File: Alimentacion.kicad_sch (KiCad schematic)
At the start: 0 parts

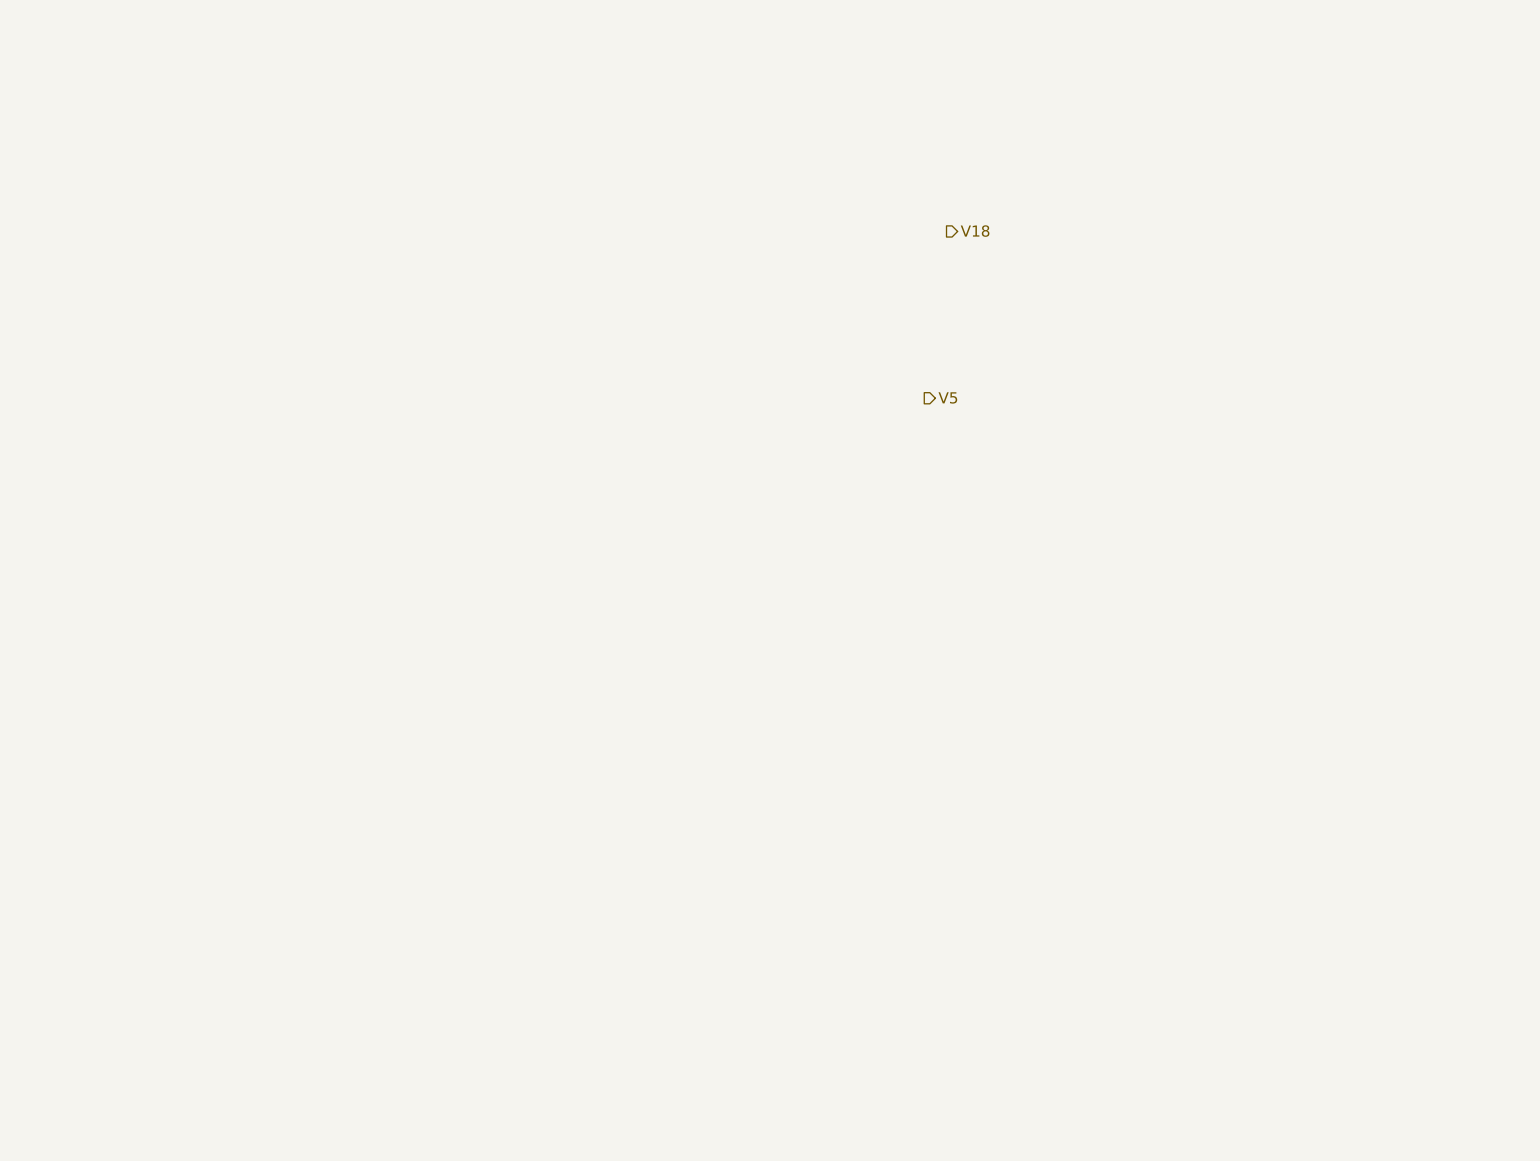
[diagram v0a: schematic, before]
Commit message: Branch Alimentacion 1.1 Modificaciones para que la alimentacion sea adecuada.
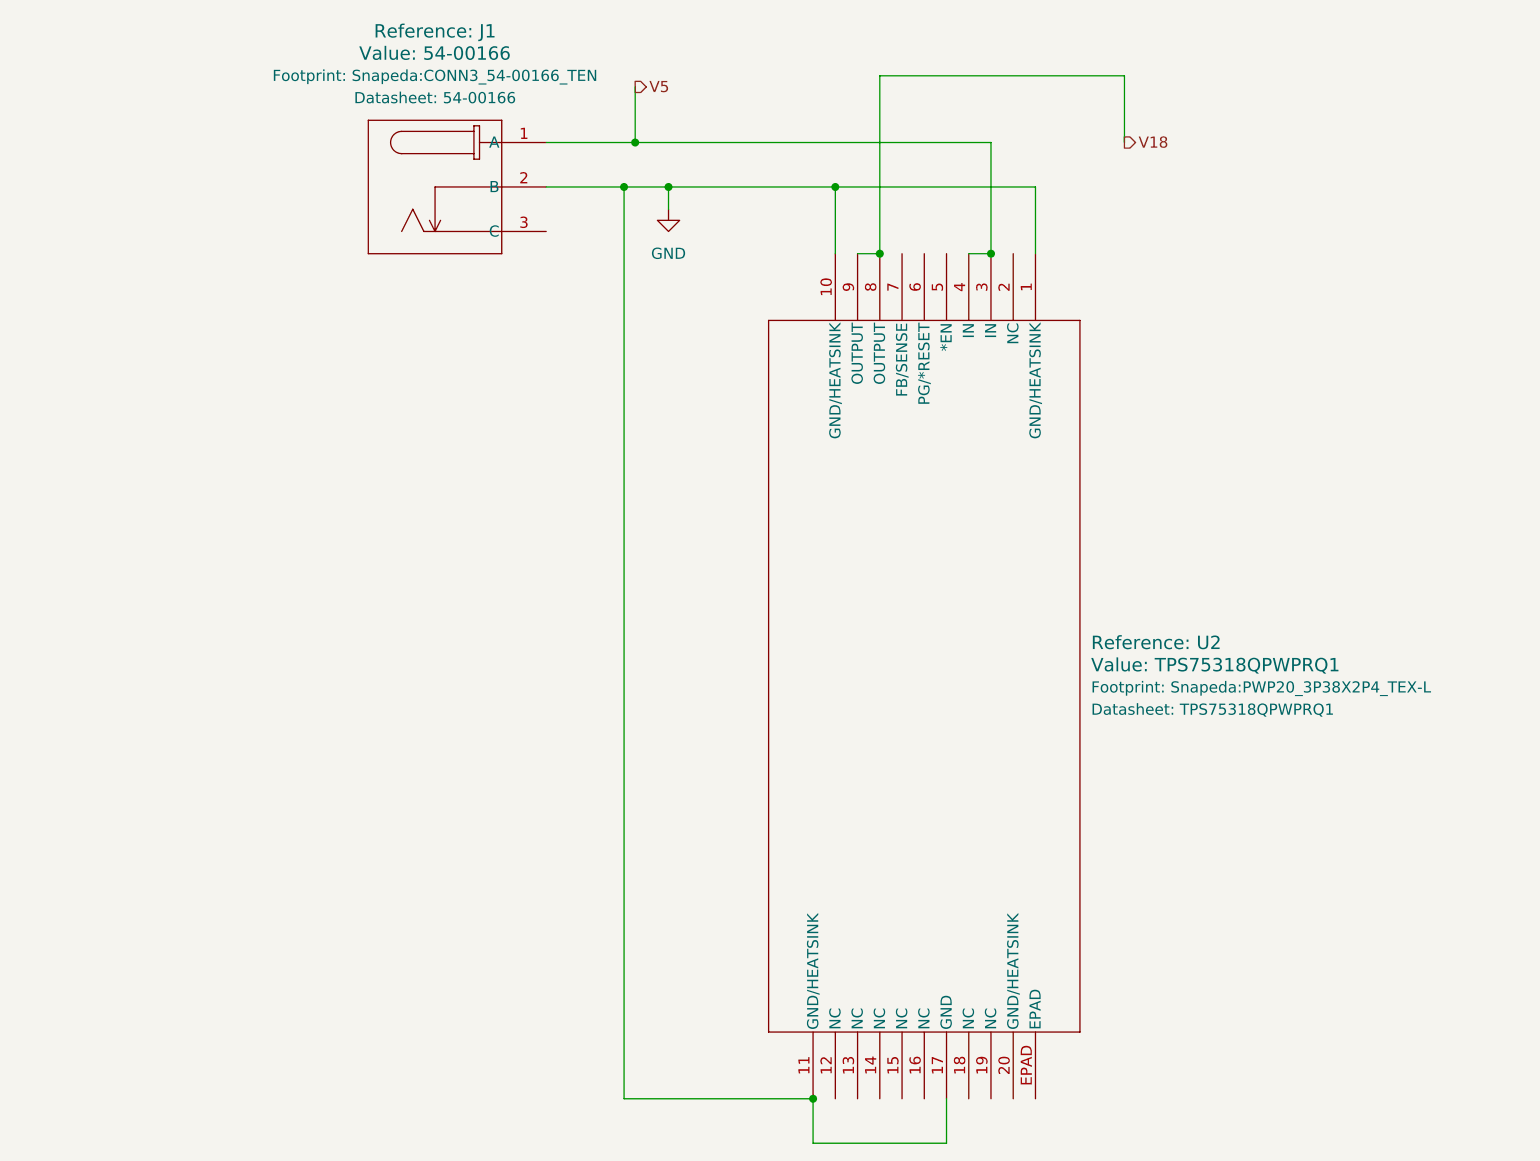
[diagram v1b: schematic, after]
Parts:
- added J1: 54-00166, Snapeda:CONN3_54-00166_TEN, symbol Snapeda:54-00166
- added U2: TPS75318QPWPRQ1, Snapeda:PWP20_3P38X2P4_TEX-L, symbol Snapeda:TPS75318QPWPRQ1
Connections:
- net V18: now also U2.8 (OUTPUT), U2.9 (OUTPUT)
- net V5: now also J1.1 (A), U2.3 (IN), U2.4 (IN)
- new net GND: J1.2 (B), U2.1 (GND/HEATSINK), U2.10 (GND/HEATSINK), U2.11 (GND/HEATSINK), U2.17 (GND)

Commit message: Alimentacion v1.2 Completamos los MPN de la hoja Alimentacion
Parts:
- J1: MPN (none) -> 54-00166
- U2: MPN (none) -> TPS75318QPWPRQ1
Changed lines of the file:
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@@
+			)
+		)
+		(property "MPN" "54-00166"
+			(at 62.23 49.53 0)
+			(hide yes)
+			(show_name no)
+			(do_not_autoplace no)
+			(effects
+				(font
+					(size 1.27 1.27)
+				)
 			)
 		)
@@
 			(do_not_autoplace no)
 			(effects
+				(font
+					(size 1.27 1.27)
+				)
+			)
+		)
+		(property "MPN" "TPS75318QPWPRQ1"
+			(at 118.11 62.23 90)
+			(hide yes)
+			(show_name no)
+			(do_not_autoplace no)
+			(effects

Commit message: -Version 1.4
Arreglos en el esquematico
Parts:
- added C4: 47u, symbol Device:C
- added R4: 100K, symbol Device:R
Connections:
- net GND: now also J1.3 (C), U2.5 (*EN), C4.2; no longer J1.2 (B), U2.1 (GND/HEATSINK), U2.10 (GND/HEATSINK), U2.11 (GND/HEATSINK)
- net V18: now also U2.7 (FB/SENSE), C4.1, R4.1
- net at U2.6 (PG/*RESET): now also R4.2
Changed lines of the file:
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@@
 	(paper "A4")
 	(junction
-		(at 71.12 54.61)
+		(at 100.33 62.23)
 		(diameter 0)
 		(color 0 0 0 0)
@@
 	)
 	(junction
-		(at 95.25 54.61)
+		(at 100.33 52.07)
 		(diameter 0)
 		(color 0 0 0 0)
@@
 	)
 	(junction
-		(at 92.71 158.75)
-		(diameter 0)
-		(color 0 0 0 0)
-	)
-	(junction
-		(at 100.33 62.23)
+		(at 118.11 41.91)
 		(diameter 0)
 		(color 0 0 0 0)
@@
 		(color 0 0 0 0)
 	)
+	(junction
+		(at 71.12 59.69)
+		(diameter 0)
+		(color 0 0 0 0)
+	)
+	(junction
+		(at 107.95 54.61)
+		(diameter 0)
+		(color 0 0 0 0)
+	)
+	(wire
+		(pts
+			(xy 97.79 62.23) (xy 100.33 62.23)
+		)
+		(stroke
+			(width 0)
+			(type default)
+		)
+	)
+	(wire
+		(pts
+			(xy 118.11 52.07) (xy 118.11 54.61)
+		)
+		(stroke
+			(width 0)
+			(type default)
+		)
+	)
 	(wire
 		(pts
@@
 	(wire
 		(pts
-			(xy 118.11 54.61) (xy 95.25 54.61)
+			(xy 62.23 59.69) (xy 71.12 59.69)
+		)
+		(stroke
+			(width 0)
+			(type default)
+		)
+	)
+	(wire
+		(pts
+			(xy 76.2 54.61) (xy 107.95 54.61)
 		)
 		(stroke
@@
 	(wire
 		(pts
-			(xy 62.23 54.61) (xy 71.12 54.61)
-		)
-		(stroke
-			(width 0)
-			(type default)
-		)
-	)
-	(wire
-		(pts
-			(xy 71.12 158.75) (xy 92.71 158.75)
-		)
-		(stroke
-			(width 0)
-			(type default)
-		)
-	)
-	(wire
-		(pts
-			(xy 118.11 62.23) (xy 118.11 54.61)
+			(xy 110.49 62.23) (xy 113.03 62.23)
+		)
+		(stroke
+			(width 0)
+			(type default)
+		)
+	)
+	(wire
+		(pts
+			(xy 71.12 59.69) (xy 71.12 54.61)
+		)
+		(stroke
+			(width 0)
+			(type default)
+		)
+	)
+	(wire
+		(pts
+			(xy 105.41 62.23) (xy 105.41 59.69)
+		)
+		(stroke
+			(width 0)
+			(type default)
+		)
+	)
+	(wire
+		(pts
+			(xy 118.11 41.91) (xy 100.33 41.91)
+		)
+		(stroke
+			(width 0)
+			(type default)
+		)
+	)
+	(wire
+		(pts
+			(xy 71.12 163.83) (xy 107.95 163.83)
 		)
 		(stroke
@@
 	(wire
 		(pts
-			(xy 97.79 62.23) (xy 100.33 62.23)
-		)
-		(stroke
-			(width 0)
-			(type default)
-		)
-	)
-	(wire
-		(pts
-			(xy 107.95 163.83) (xy 92.71 163.83)
-		)
-		(stroke
-			(width 0)
-			(type default)
-		)
-	)
-	(wire
-		(pts
-			(xy 76.2 54.61) (xy 95.25 54.61)
+			(xy 107.95 62.23) (xy 107.95 54.61)
+		)
+		(stroke
+			(width 0)
+			(type default)
+		)
+	)
+	(wire
+		(pts
+			(xy 118.11 41.91) (xy 118.11 44.45)
 		)
 		(stroke
@@
 	(wire
 		(pts
-			(xy 100.33 41.91) (xy 100.33 62.23)
-		)
-		(stroke
-			(width 0)
-			(type default)
-		)
-	)
-	(wire
-		(pts
-			(xy 128.27 41.91) (xy 100.33 41.91)
-		)
-		(stroke
-			(width 0)
-			(type default)
-		)
-	)
-	(wire
-		(pts
-			(xy 110.49 62.23) (xy 113.03 62.23)
+			(xy 107.95 54.61) (xy 118.11 54.61)
+		)
+		(stroke
+			(width 0)
+			(type default)
+		)
+	)
+	(wire
+		(pts
+			(xy 100.33 41.91) (xy 100.33 52.07)
+		)
+		(stroke
+			(width 0)
+			(type default)
+		)
+	)
+	(wire
+		(pts
+			(xy 128.27 41.91) (xy 118.11 41.91)
+		)
+		(stroke
+			(width 0)
+			(type default)
+		)
+	)
+	(wire
+		(pts
+			(xy 100.33 52.07) (xy 100.33 62.23)
 		)
 		(stroke
@@
 	(wire
 		(pts
-			(xy 92.71 163.83) (xy 92.71 158.75)
-		)
-		(stroke
-			(width 0)
-			(type default)
-		)
-	)
-	(wire
-		(pts
 			(xy 128.27 49.53) (xy 128.27 41.91)
 		)
@@
 	(wire
 		(pts
-			(xy 71.12 158.75) (xy 71.12 54.61)
-		)
-		(stroke
-			(width 0)
-			(type default)
-		)
-	)
-	(wire
-		(pts
-			(xy 95.25 54.61) (xy 95.25 62.23)
+			(xy 100.33 62.23) (xy 102.87 62.23)
+		)
+		(stroke
+			(width 0)
+			(type default)
+		)
+	)
+	(wire
+		(pts
+			(xy 71.12 59.69) (xy 71.12 163.83)
+		)
+		(stroke
+			(width 0)
+			(type default)
+		)
+	)
+	(wire
+		(pts
+			(xy 100.33 52.07) (xy 105.41 52.07)
 		)
 		(stroke
@@
 	)
 	(symbol
+		(lib_id "Device:C")
+		(at 118.11 48.26 0)
+		(unit 1)
+		(body_style 1)
+		(exclude_from_sim no)
+		(in_bom yes)
+		(on_board yes)
+		(in_pos_files yes)
+		(dnp no)
+		(fields_autoplaced yes)
+		(property "Reference" "C4"
+			(at 121.92 46.9899 0)
+			(show_name no)
+			(do_not_autoplace no)
+			(effects
+				(font
+					(size 1.27 1.27)
+				)
+				(justify left)
+			)
+		)
+		(property "Value" "47u"
+			(at 121.92 49.5299 0)
+			(show_name no)
+			(do_not_autoplace no)
+			(effects
+				(font
+					(size 1.27 1.27)
+				)
+				(justify left)
+			)
+		)
+		(property "Footprint" ""
+			(at 119.0752 52.07 0)
+			(hide yes)
+			(show_name no)
+			(do_not_autoplace no)
+			(effects
+				(font
+					(size 1.27 1.27)
+				)
+			)
+		)
+		(property "Datasheet" ""
+			(at 118.11 48.26 0)
+			(hide yes)
+			(show_name no)
+			(do_not_autoplace no)
+			(effects
+				(font
+					(size 1.27 1.27)
+				)
+			)
+		)
+		(property "Description" "Unpolarized capacitor"
+			(at 118.11 48.26 0)
+			(hide yes)
+			(show_name no)
+			(do_not_autoplace no)
+			(effects
+				(font
+					(size 1.27 1.27)
+				)
+			)
+		)
+		(pin "2"
+		)
+		(pin "1"
+		)
+		(instances
+			(project "Tarea_2"
+				(path "/9f5ae3b6-454f-40a7-b9eb-0aa1aaaab031/3003bad4-0810-403b-9c7b-0bf87e8d2e85"
+					(reference "C4")
+					(unit 1)
+				)
+			)
+		)
+	)
+	(symbol
 		(lib_id "power:GND")
 		(at 76.2 57.15 0)
@@
 					(unit 1)
 				)
+			)
+		)
+	)
+	(symbol
+		(lib_id "Device:R")
+		(at 105.41 55.88 0)
+		(unit 1)
+		(body_style 1)
+		(exclude_from_sim no)
+		(in_bom yes)
+		(on_board yes)
+		(in_pos_files yes)
+		(dnp no)
+		(fields_autoplaced yes)
+		(property "Reference" "R4"
+			(at 107.95 54.6099 0)
+			(show_name no)
+			(do_not_autoplace no)
+			(effects
+				(font
+					(size 1.27 1.27)
+				)
+				(justify left)
+			)
+		)
+		(property "Value" "100K"
+			(at 107.95 57.1499 0)
+			(show_name no)
+			(do_not_autoplace no)
+			(effects
+				(font
+					(size 1.27 1.27)
+				)
+				(justify left)
+			)
+		)
+		(property "Footprint" ""
+			(at 103.632 55.88 90)
+			(hide yes)
+			(show_name no)
+			(do_not_autoplace no)
+			(effects
+				(font
+					(size 1.27 1.27)
+				)
+			)
+		)
+		(property "Datasheet" ""
+			(at 105.41 55.88 0)
+			(hide yes)
+			(show_name no)
+			(do_not_autoplace no)
+			(effects
+				(font
+					(size 1.27 1.27)
+				)
+			)
+		)
+		(property "Description" "Resistor"
+			(at 105.41 55.88 0)
+			(hide yes)
+			(show_name no)
+			(do_not_autoplace no)
+			(effects
+				(font
+					(size 1.27 1.27)
+				)
+			)
+		)
+		(pin "2"
+		)
+		(pin "1"
+		)
+		(instances
+			(project "Tarea_2"
+				(path "/9f5ae3b6-454f-40a7-b9eb-0aa1aaaab031/3003bad4-0810-403b-9c7b-0bf87e8d2e85"
+					(reference "R4")
+					(unit 1)
+				)

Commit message: Version 1.5
Añadidos condensadores de desacoplo en el esquematico.
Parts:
- added C5: 220n, symbol Device:C
- added C6: 47u, symbol Device:C
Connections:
- net GND: now also C5.2, C6.2
- net V5: now also C5.1, C6.1
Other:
- moved on the sheet: Reference: J1

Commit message: - Primer commit de la rama
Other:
- moved on the sheet: C4
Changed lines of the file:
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@@
+	)
+	(junction
+		(at 86.36 54.61)
+		(diameter 0)
+		(color 0 0 0 0)
 	)
 	(junction
@@
 	)
 	(junction
+		(at 100.33 41.91)
+		(diameter 0)
+		(color 0 0 0 0)
+	)
+	(junction
 		(at 57.15 59.69)
 		(diameter 0)
@@
 	)
 	(junction
-		(at 118.11 41.91)
-		(diameter 0)
-		(color 0 0 0 0)
-	)
-	(junction
 		(at 76.2 54.61)
 		(diameter 0)
@@
 		(color 0 0 0 0)
 	)
-	(junction
-		(at 107.95 54.61)
-		(diameter 0)
-		(color 0 0 0 0)
-	)
 	(wire
 		(pts
@@
 	(wire
 		(pts
-			(xy 118.11 52.07) (xy 118.11 54.61)
+			(xy 86.36 41.91) (xy 100.33 41.91)
 		)
 		(stroke
@@
 	(wire
 		(pts
-			(xy 76.2 54.61) (xy 107.95 54.61)
+			(xy 76.2 54.61) (xy 86.36 54.61)
 		)
 		(stroke
@@
 	(wire
 		(pts
-			(xy 118.11 41.91) (xy 100.33 41.91)
+			(xy 100.33 41.91) (xy 128.27 41.91)
 		)
 		(stroke
@@
 	(wire
 		(pts
+			(xy 86.36 54.61) (xy 107.95 54.61)
+		)
+		(stroke
+			(width 0)
+			(type default)
+		)
+	)
+	(wire
+		(pts
 			(xy 46.99 59.69) (xy 57.15 59.69)
 		)
@@
 	(wire
 		(pts
-			(xy 118.11 41.91) (xy 118.11 44.45)
+			(xy 86.36 41.91) (xy 86.36 46.99)
 		)
 		(stroke
@@
 	(wire
 		(pts
-			(xy 107.95 54.61) (xy 118.11 54.61)
-		)
-		(stroke
-			(width 0)
-			(type default)
-		)
-	)
-	(wire
-		(pts
 			(xy 100.33 41.91) (xy 100.33 52.07)
-		)
-		(stroke
-			(width 0)
-			(type default)
-		)
-	)
-	(wire
-		(pts
-			(xy 128.27 41.91) (xy 118.11 41.91)
 		)
 		(stroke
@@
 	(symbol
 		(lib_id "Device:C")
-		(at 118.11 48.26 0)
+		(at 86.36 50.8 0)
 		(unit 1)
 		(body_style 1)
@@
 		(fields_autoplaced yes)
 		(property "Reference" "C4"
-			(at 121.92 46.9899 0)
+			(at 90.17 49.5299 0)
 			(show_name no)
 			(do_not_autoplace no)
@@
 		)
 		(property "Value" "47u"
-			(at 121.92 49.5299 0)
+			(at 90.17 52.0699 0)
 			(show_name no)
 			(do_not_autoplace no)
@@
 		)
 		(property "Footprint" ""
-			(at 119.0752 52.07 0)
+			(at 87.3252 54.61 0)
 			(hide yes)
 			(show_name no)
@@
 		)
 		(property "Datasheet" ""
-			(at 118.11 48.26 0)
+			(at 86.36 50.8 0)
 			(hide yes)
 			(show_name no)
@@
 		)
 		(property "Description" "Unpolarized capacitor"
-			(at 118.11 48.26 0)
-			(hide yes)
-			(show_name no)
+			(at 86.36 50.8 0)
+			(hide yes)
+			(show_name no)
